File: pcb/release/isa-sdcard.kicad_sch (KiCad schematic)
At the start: 52 parts, among them J1 Micro_SD_Card_Det1, J2 Bus_ISA_8bit_AB_Rev0, SW1 ADDR SEL, U1 74HC00, U10 74HC74, U11 74HC08, U12 74HC04, U13 74HC74, U16 AMS1117-3.3, U2 74HCT32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

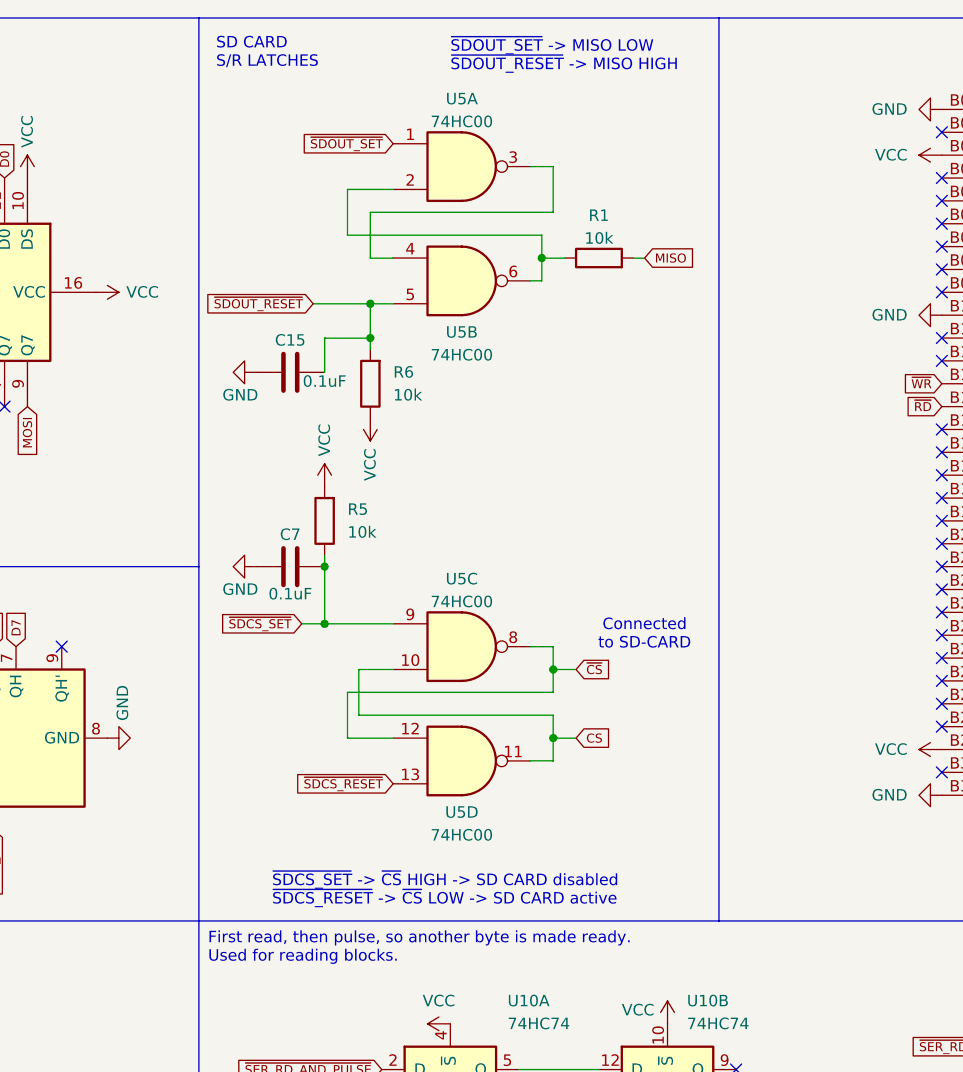
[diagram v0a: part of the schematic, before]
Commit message: Removing delay lines
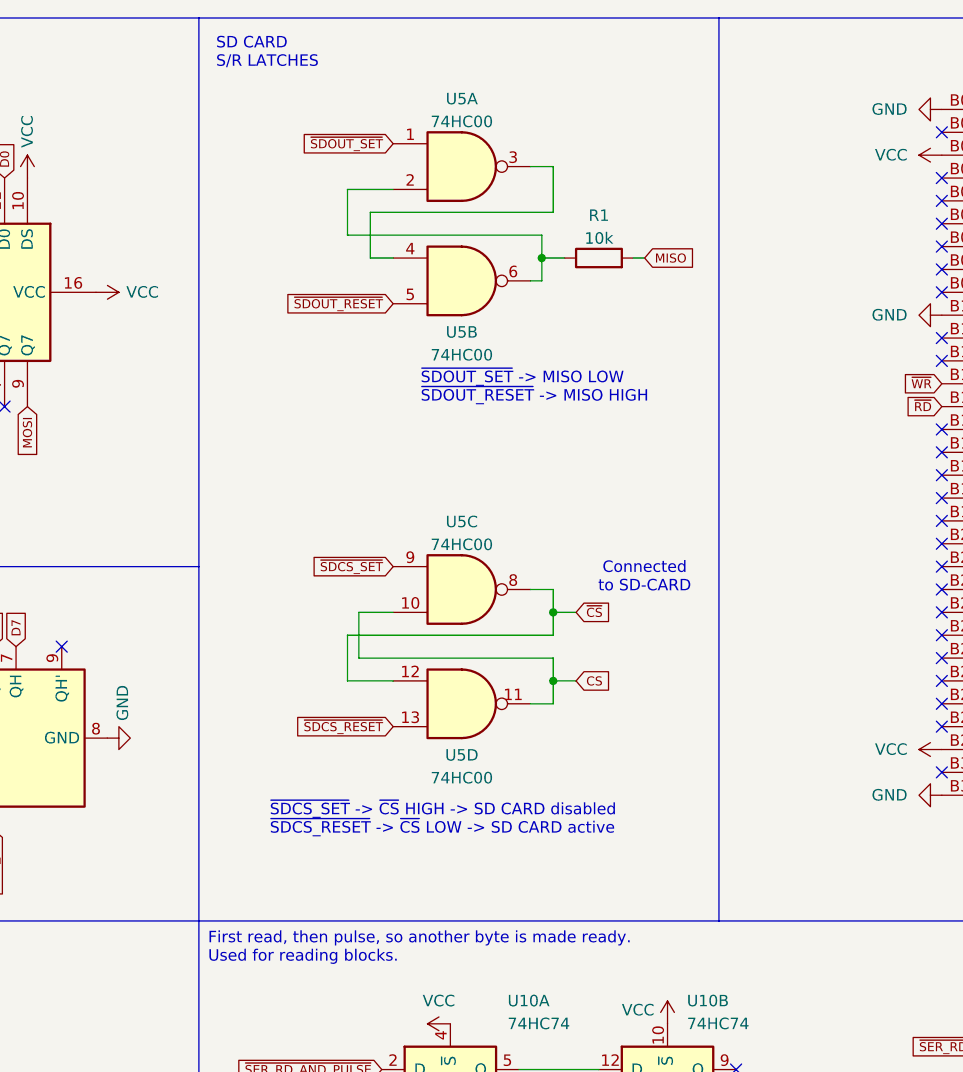
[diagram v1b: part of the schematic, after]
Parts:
- removed C15, C7: 0.1uF, Capacitor_SMD:C_0805_2012Metric, symbol Device:C
- removed R5, R6: 10k, Resistor_SMD:R_0805_2012Metric, symbol Device:R
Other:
- moved on the sheet: U5C, U5D

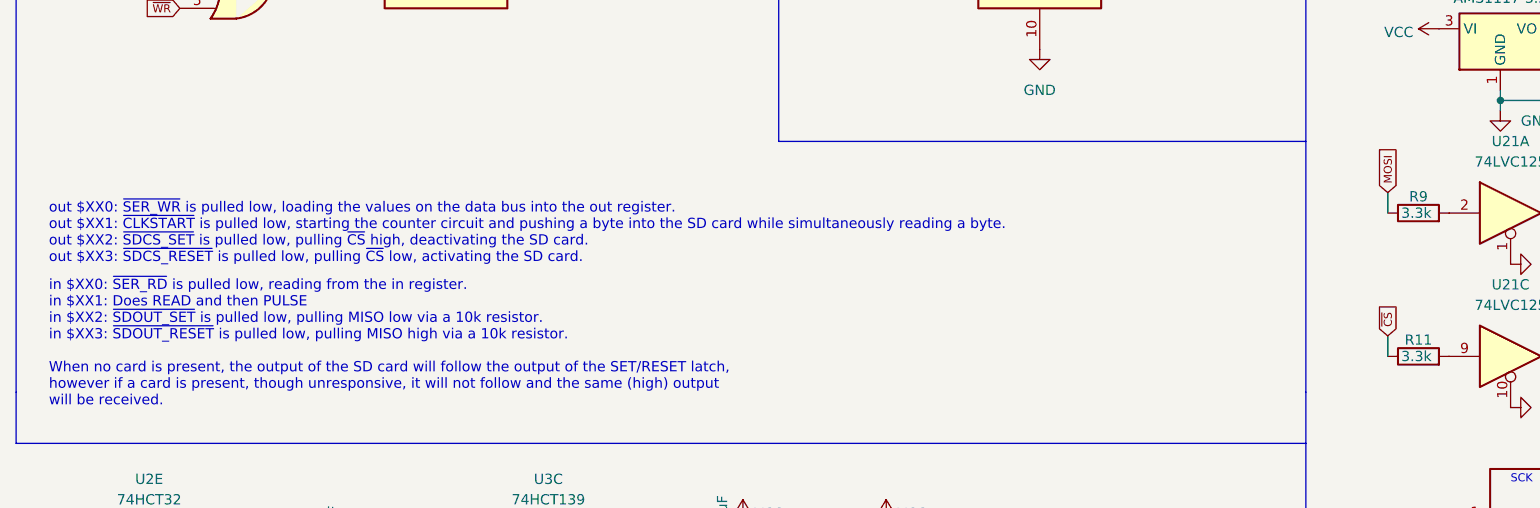
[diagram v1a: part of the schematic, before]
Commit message: Improving schematic, improving sd commands and making cross-compilation more convenient
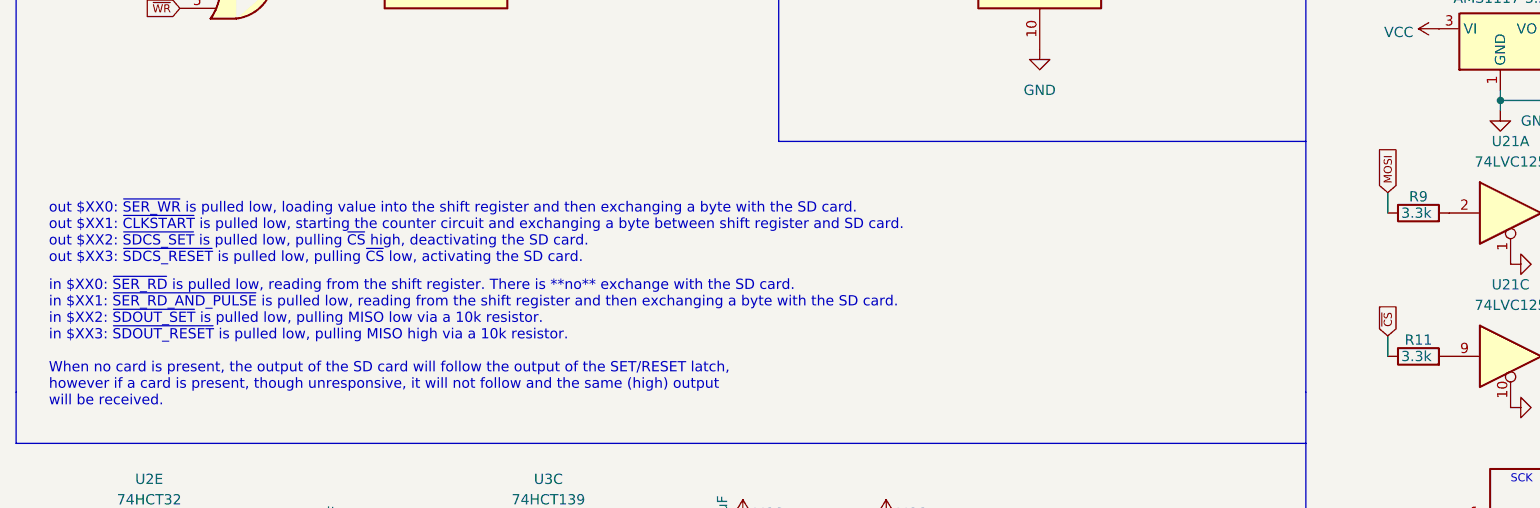
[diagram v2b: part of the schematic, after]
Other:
- note added: "in $XX0: ~{SER_RD} is pulled low, reading from the shift register. There is **no** exchange with the SD card. in $XX1: ~{SER_RD_AND_PULSE} is pulled low, reading from the shift register and then exchanging a byte with the SD card. in $XX2: ~{SDOUT_SET} is pulled low, pulling MISO low via a 10k resistor. in $XX3: ~{SDOUT_RESET} is pulled low, pulling MISO high via a 10k resistor. When no card is p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"
- note added: "out $XX0: ~{SER_WR} is pulled low, loading value into the shift register and then exchanging a byte with the SD card. out $XX1: ~{CLKSTART} is pulled low, starting the counter circuit and exchanging a byte between shift register and SD card. out $XX2: ~{SDCS_SET} is pulled low, pulling ~{CS} high, deactivating the SD card. out $XX3: ~{SDCS_RESET} is pulled low, pulling ~{CS} low, activating the S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"
- note removed: "in $XX0: ~{SER_RD} is pulled low, reading from the in register. in $XX1: Does READ and then PULSE in $XX2: ~{SDOUT_SET} is pulled low, pulling MISO low via a 10k resistor. in $XX3: ~{SDOUT_RESET} is pulled low, pulling MISO high via a 10k resistor. When no card is present, the output of the SD card will follow the output of the SET/RESET latch, however if a card is present, though unresponsive, i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"
- note removed: "out $XX0: ~{SER_WR} is pulled low, loading the values on the data bus into the out register. out $XX1: ~{CLKSTART} is pulled low, starting the counter circuit and pushing a byte into the SD card while simultaneously reading a byte. out $XX2: ~{SDCS_SET} is pulled low, pulling ~{CS} high, deactivating the SD card. out $XX3: ~{SDCS_RESET} is pulled low, pulling ~{CS} low, activating the SD card."
